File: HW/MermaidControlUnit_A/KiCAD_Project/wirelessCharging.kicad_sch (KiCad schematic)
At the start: 39 parts, among them J12 Coil_1, J13 Coil_2, U10 BQ51013C-Q1

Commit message: schematic added, folder structure updated
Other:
- company: (none) -> Aurora Dreams Mermaids
- title: (none) -> Mermaid Control Unit
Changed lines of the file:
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@@
 	(generator_version "8.0")
 	(paper "A4")
+	(title_block
+		(title "Mermaid Control Unit")
+		(date "2025-02-04")
+		(rev "A")
+		(company "Aurora Dreams Mermaids")
+		(comment 1 "Designed by: Ondrej Ruzicka")
+		(comment 4 "Wireless Charging")
+	)
 	(junction
 		(at 54.61 95.25)

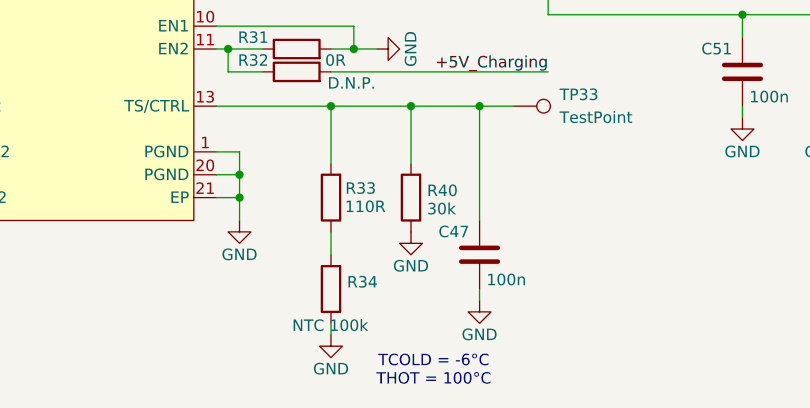
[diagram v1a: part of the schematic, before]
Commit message: BQ NTC retuned
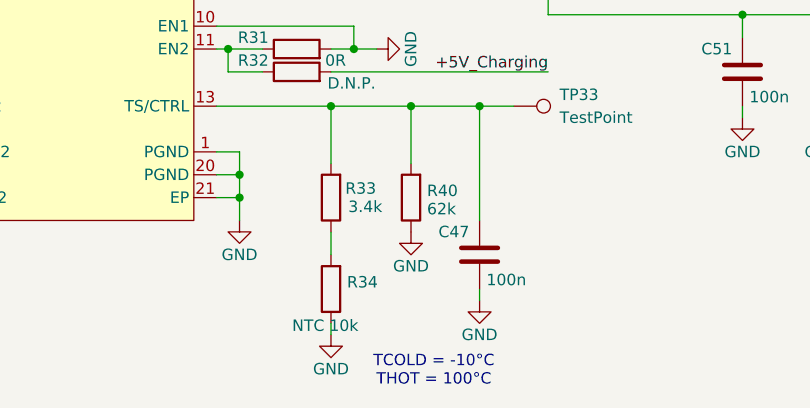
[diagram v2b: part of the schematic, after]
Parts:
- R33: value 110R -> 3.4k; Part Number 0603WAF1100T5E -> 0603WAF4301T5E
- R34: value NTC 100k -> NTC 10k; Part Number NCU18WF104F6SRB -> NTCG163JF103FTDS
- R40: value 30k -> 62k; Part Number 0603WAF3002T5E -> 0603WAF6202T5E
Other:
- note added: "TCOLD = -10°C THOT = 100°C"
- note removed: "TCOLD = -6°C THOT = 100°C"
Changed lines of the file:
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@@
 		)
 	)
-	(text "TCOLD = -6°C\nTHOT = 100°C"
+	(text "TCOLD = -10°C\nTHOT = 100°C"
 		(exclude_from_sim no)
 		(at 179.07 137.414 0)
@@
 			)
 		)
-		(property "Value" "NTC 100k"
+		(property "Value" "NTC 10k"
 			(at 163.322 132.334 0)
 			(effects
@@
 			)
 		)
-		(property "Part Number" "NCU18WF104F6SRB"
+		(property "Part Number" "NTCG163JF103FTDS"
 			(at 167.64 128.27 0)
 			(effects
@@
 			)
 		)
-		(property "Value" "30k"
+		(property "Value" "62k"
 			(at 178.308 119.38 0)
 			(effects
@@
 			)
 		)
-		(property "Part Number" "0603WAF3002T5E "
+		(property "Part Number" "0603WAF6202T5E  "
 			(at 176.53 118.11 0)
 			(effects
@@
 			)
 		)
-		(property "Value" "110R"
+		(property "Value" "3.4k"
 			(at 171.45 119.126 0)
 			(effects
@@
 			)
 		)
-		(property "Part Number" "0603WAF1100T5E "
+		(property "Part Number" "0603WAF4301T5E  "
 			(at 167.64 118.11 0)
 			(effects
